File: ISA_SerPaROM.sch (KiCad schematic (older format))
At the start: 91 parts, among them J1 ISA BUS, J10 Parallel Port, J11 Serial 4 IDC, J12 Serial 3 IDC, J13 UART4_SEL, J14 ROM Config, J2 ADDR_IRQ, J3 UART1_SEL, J4 UART2_SEL, J5 ADDR, J6 Serial 2 IDC, J7 Serial 1 DB9, J8 UART3_SEL, J9 Parport IRQ Select, U1 74HCT138, U11 74LS30, U12 74LS86, U13 74LS02, U14 74LS155, U15 74LS245, U16 74LS174, U17 74LS374, U18 74LS05, U19 74LS125, U2 74HCT138, U20 74LS240, U21 74LS244, U23 16C554, U24 74HCT32, U25 GD75232N, U26 GD75232N, U27 SST39SF040, U28 74HCT688, U5 GD75232N, U6 GD75232N, X1 1.8432Mhz

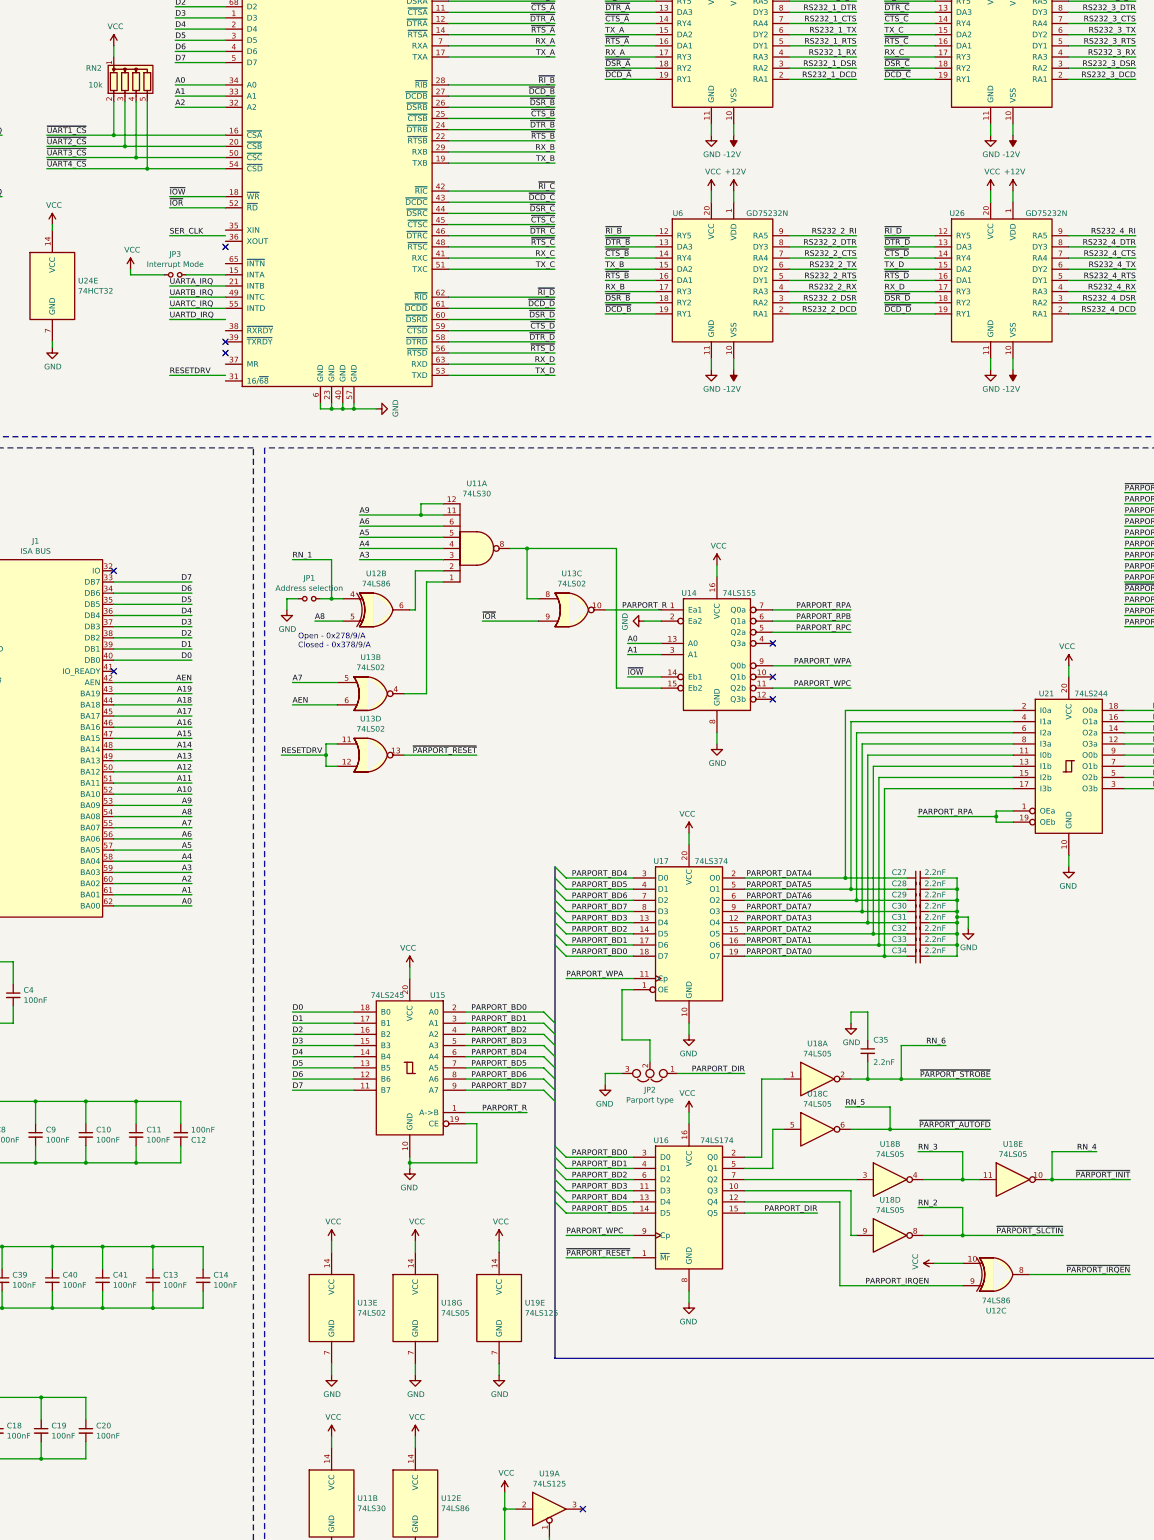
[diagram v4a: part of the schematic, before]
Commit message: Added LED bar and moved serial leds
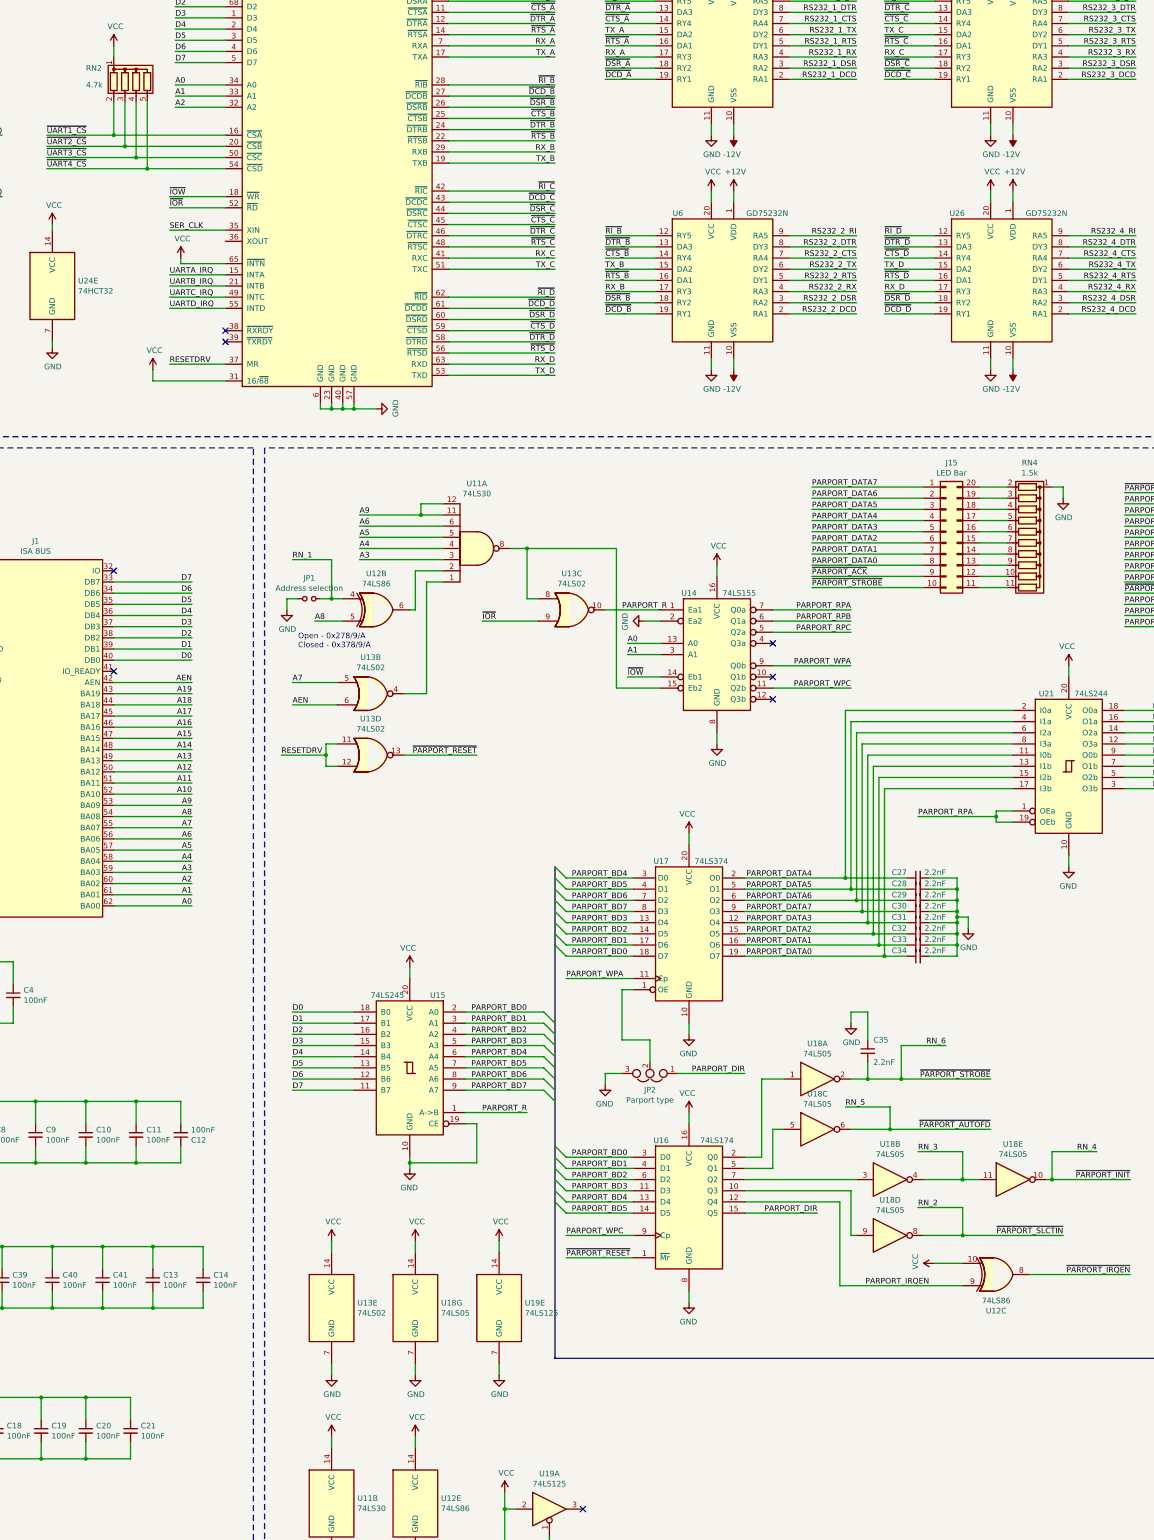
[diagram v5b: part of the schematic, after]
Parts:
- removed JP3: Interrupt Mode, Connector_PinHeader_2.54mm:PinHeader_1x02_P2.54mm_Vertical, symbol Device:Jumper_NO_Small
- added C21: 100nF, Capacitor_THT:C_Disc_D6.0mm_W2.5mm_P5.00mm, symbol Device:C_Small
- added J15: LED Bar, Package_DIP:DIP-20_W7.62mm_Socket_LongPads, symbol Connector_Generic:Conn_02x10_Counter_Clockwise
- added RN4: 1.5k, Resistor_THT:R_Array_SIP11, symbol Device:R_Network10
- R10, R3, R4, R5, R6, R7, R8, R9: footprint Resistor_THT:R_Axial_DIN0207_L6.3mm_D2.5mm_P10.16mm_Horizontal -> Resistor_THT:R_Axial_DIN0204_L3.6mm_D1.6mm_P5.08mm_Horizontal
- RN2: value 10k -> 4.7k
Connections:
- net GND: now also C21.2, RN4.1 (common)
- net PARPORT_DATA0: now also J15.8 (Pin_8)
- net PARPORT_DATA1: now also J15.7 (Pin_7)
- net PARPORT_DATA2: now also J15.6 (Pin_6)
- net PARPORT_DATA3: now also J15.5 (Pin_5)
- net PARPORT_DATA4: now also J15.4 (Pin_4)
- net PARPORT_DATA5: now also J15.3 (Pin_3)
- net PARPORT_DATA6: now also J15.2 (Pin_2)
- net PARPORT_DATA7: now also J15.1 (Pin_1)
- net RESETDRV: now also U23.37 (MR)
- net RN_6: now also J15.10 (Pin_10)
- net RN_7: now also J15.9 (Pin_9)
- net SER_CLK: now also U23.35 (XIN)
- net UARTA_IRQ: now also U23.15 (INTA); no longer U23.21 (INTB)
- net UARTB_IRQ: now also U23.21 (INTB); no longer U23.49 (INTC)
- net UARTC_IRQ: now also U23.49 (INTC); no longer U23.55 (INTD)
- net UARTD_IRQ: now also U23.55 (INTD)
- net VCC: now also U23.31 (16/~68), U23.65 (~INTN), C21.1
- new net: J15.12 (Pin_12), RN4.10 (R9)
- new net: J15.11 (Pin_11), RN4.11 (R10)
- new net: J15.20 (Pin_20), RN4.2 (R1)
- new net: J15.19 (Pin_19), RN4.3 (R2)
- new net: J15.18 (Pin_18), RN4.4 (R3)
- new net: J15.17 (Pin_17), RN4.5 (R4)
- new net: J15.16 (Pin_16), RN4.6 (R5)
- new net: J15.15 (Pin_15), RN4.7 (R6)
- new net: J15.14 (Pin_14), RN4.8 (R7)
- new net: J15.13 (Pin_13), RN4.9 (R8)
- no-connect marks 37 -> 36
